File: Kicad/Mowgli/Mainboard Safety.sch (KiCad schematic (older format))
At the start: 3 parts, among them U3 4075

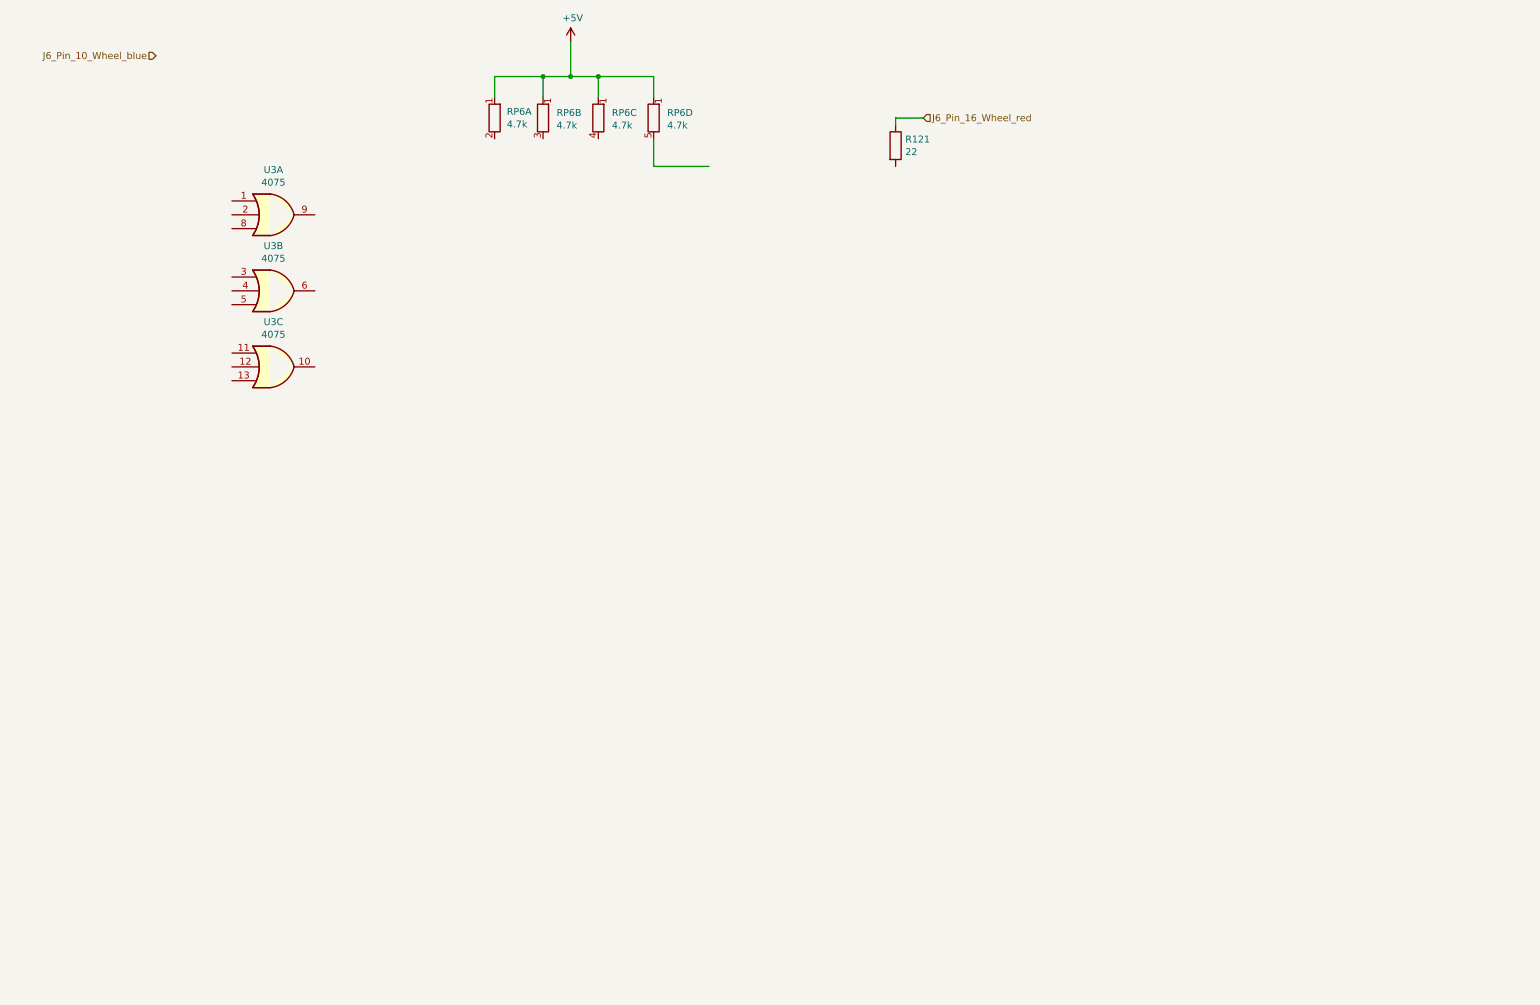
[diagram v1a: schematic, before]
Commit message: reversed mechanical tilt and accelerometer circuit
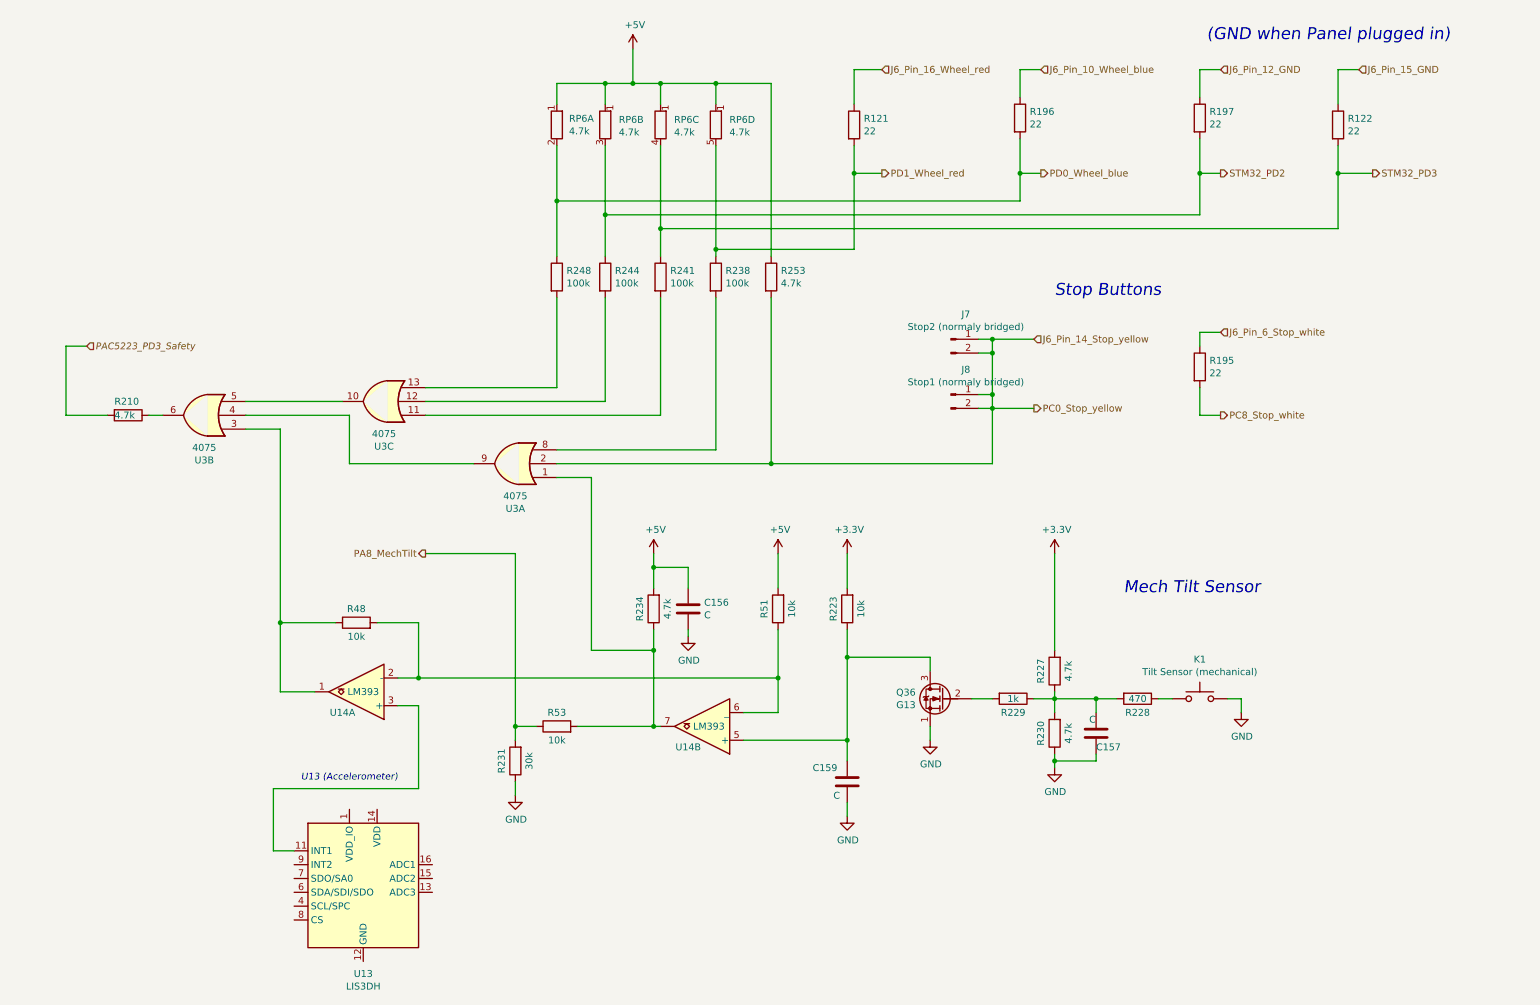
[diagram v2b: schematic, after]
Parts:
- added C156, C157, C159: C, symbol Device:C
- added J7: Stop2 (normaly bridged), symbol Connector:Conn_01x02_Male
- added J8: Stop1 (normaly bridged), symbol Connector:Conn_01x02_Male
- added K1: Tilt Sensor (mechanical), symbol Switch:SW_Push
- added Q36: G13, symbol Device:Q_NMOS_SGD
- added R122, R195, R196, R197: 22, symbol Device:R
- added R210, R227, R230, R234, R253: 4.7k, symbol Device:R
- added R223, R48, R51, R53: 10k, symbol Device:R
- added R228: 470, symbol Device:R
- added R229: 1k, symbol Device:R
- added R231: 30k, symbol Device:R
- added R238, R241, R244, R248: 100k, symbol Device:R
- added U13: LIS3DH, Package_LGA:LGA-16_3x3mm_P0.5mm_LayoutBorder3x5y, symbol Sensor_Motion:LIS3DH
- added U14: LM393, symbol Comparator:LM393
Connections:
- net labels added: +3.3V, GND, J6_Pin_12_GND, J6_Pin_14_Stop_yellow, J6_Pin_15_GND, J6_Pin_6_Stop_white, PA8_MechTilt, PAC5223_PD3_Safety, PC0_Stop_yellow, PC8_Stop_white, PD0_Wheel_blue, PD1_Wheel_red, STM32_PD2, STM32_PD3
- wire segments 13 -> 135
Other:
- note added: "(GND when Panel plugged in)"
- note added: "Mech Tilt Sensor"
- note added: "Stop Buttons"
- note added: "U13 (Accelerometer)"
- moved on the sheet: R121, RP6A, RP6B, RP6C, RP6D, U3A, U3B, U3C

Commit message: added Panel Eliminator
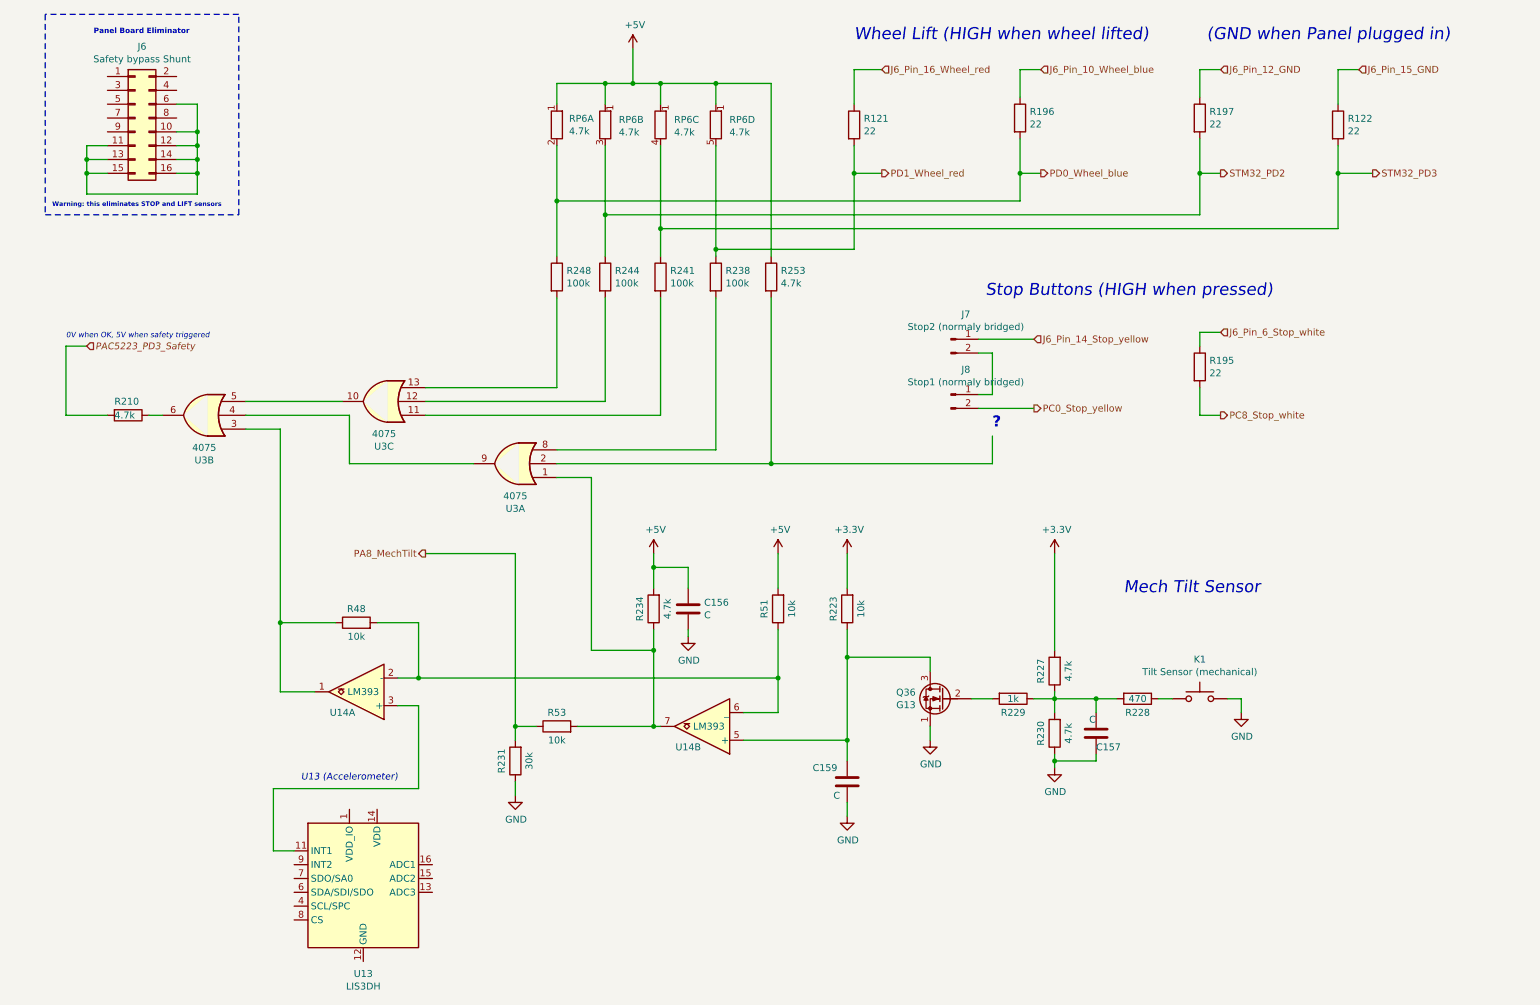
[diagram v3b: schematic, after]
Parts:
- added J6: Safety bypass Shunt, symbol Connector_Generic:Conn_02x08_Odd_Even
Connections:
- wire segments 135 -> 148
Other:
- note added: "0V when OK, 5V when safety triggered"
- note added: "?"
- note added: "Panel Board Eliminator"
- note added: "Stop Buttons (HIGH when pressed)"
- note added: "Warning: this eliminates STOP and LIFT sensors"
- note added: "Wheel Lift (HIGH when wheel lifted)"
- note removed: "Stop Buttons"
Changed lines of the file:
@@
 	7500 3050 7600 3050
 Wire Wire Line
-	7500 2950 7600 2950
-Wire Wire Line
-	7600 3050 7600 2950
-Connection ~ 7600 2950
-Wire Wire Line
-	7600 2950 7900 2950
-Wire Wire Line
 	7600 3050 7600 3350
 Wire Wire Line
 	7600 3350 7500 3350
-Connection ~ 7600 3050
 Text HLabel 7900 3450 2    50   Output ~ 0
 PC0_Stop_yellow
-Wire Wire Line
-	7900 3450 7600 3450
 $Comp
 L Device:R R253
@@
 	1    0    0    -1
 $EndComp
-Connection ~ 7600 3450
 $Comp
 L Device:R R238
@@
 $EndComp
 Wire Wire Line
-	7600 3450 7600 3850
-Wire Wire Line
 	4450 3850 6000 3850
 Wire Wire Line
@@
 Wire Wire Line
 	5200 2150 10100 2150
-Text Notes 8050 2650 0    87   Italic 0
-Stop Buttons
-Wire Wire Line
-	7600 3350 7600 3450
-Connection ~ 7600 3350
-Wire Wire Line
-	7500 3450 7600 3450
+Text Notes 7550 2650 0    87   Italic 0
+Stop Buttons (HIGH when pressed)
 Wire Wire Line
 	3500 4500 4150 4500
@@
 Wire Wire Line
 	900  3500 1200 3500
+Text Notes 900  2950 0    39   Italic 0
+0V when OK, 5V when safety triggered
+Wire Wire Line
+	7500 2950 7900 2950
+Wire Wire Line
+	7500 3450 7900 3450
+Wire Wire Line
+	7600 3650 7600 3850
+Text Notes 7600 3600 0    79   ~ 16
+?
+Text Notes 6600 800  0    87   Italic 0
+Wheel Lift (HIGH when wheel lifted)
+$Comp
+L Connector_Generic:Conn_02x08_Odd_Even J6
+U 1 1 62E3115A
+P 1400 1350
+F 0 "J6" H 1450 1867 50  0000 C CNN
+F 1 "Safety bypass Shunt" H 1450 1776 50  0000 C CNN
+F 2 "" H 1400 1350 50  0001 C CNN
+F 3 "~" H 1400 1350 50  0001 C CNN
+	1    1400 1350
+	1    0    0    -1
+$EndComp
+Wire Wire Line
+	1700 1450 1850 1450
+Wire Wire Line
+	1850 1450 1850 1550
+Wire Wire Line
+	1850 1750 1700 1750
+Wire Wire Line
+	1700 1650 1850 1650
+Connection ~ 1850 1650
+Wire Wire Line
+	1850 1650 1850 1750
+Wire Wire Line
+	1700 1550 1850 1550
+Connection ~ 1850 1550
+Wire Wire Line
+	1850 1550 1850 1650
+Wire Wire Line
+	1700 1250 1850 1250
+Wire Wire Line
+	1850 1250 1850 1450
+Connection ~ 1850 1450
+Wire Wire Line
+	1200 1550 1050 1550
+Wire Wire Line
+	1050 1550 1050 1650
+Wire Wire Line
+	1050 1750 1200 1750
+Wire Wire Line
+	1200 1650 1050 1650
+Connection ~ 1050 1650
+Wire Wire Line
+	1050 1650 1050 1750
+Wire Wire Line
+	1050 1750 1050 1900
+Wire Wire Line
+	1050 1900 1850 1900
+Wire Wire Line
+	1850 1900 1850 1750
+Connection ~ 1050 1750
+Connection ~ 1850 1750
+Text Notes 1100 750  0    39   ~ 8
+Panel Board Eliminator
+Wire Notes Line
+	750  600  750  2050
+Wire Notes Line
+	750  2050 2150 2050
+Wire Notes Line
+	2150 2050 2150 600
+Wire Notes Line
+	2150 600  750  600
+Text Notes 800  2000 0    33   ~ 7
+Warning: this eliminates STOP and LIFT sensors
 $EndSCHEMATC

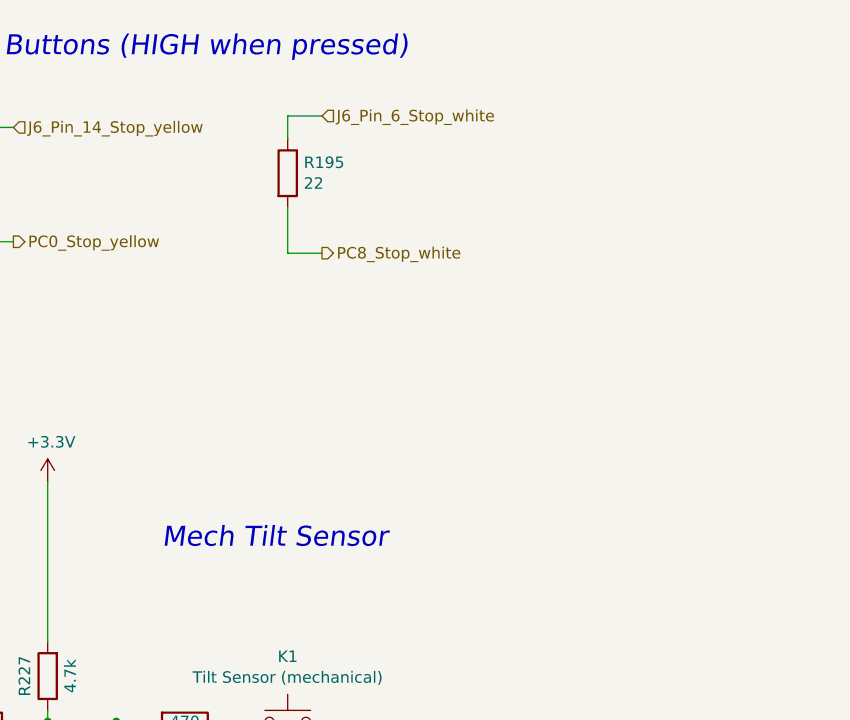
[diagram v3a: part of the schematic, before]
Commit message: R195 is not populated on all boards, (white hall sensor cable for stop button)
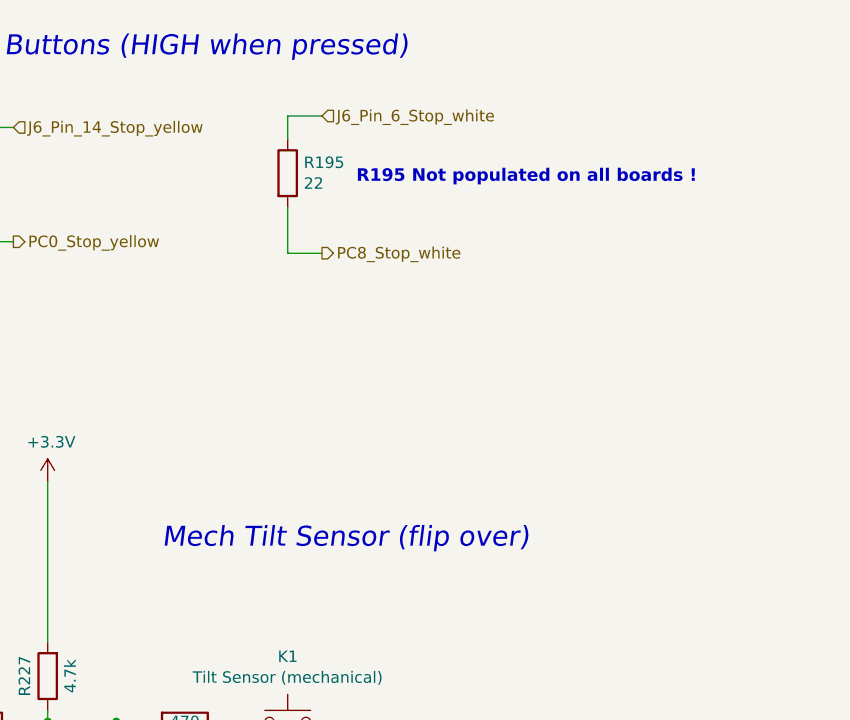
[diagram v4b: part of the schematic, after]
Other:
- note added: "Mech Tilt Sensor (flip over)"
- note added: "R195 Not populated on all boards !"
- note removed: "Mech Tilt Sensor"
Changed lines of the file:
@@
 	8050 4500 8050 5200
 Text Notes 8550 4800 0    87   Italic 0
-Mech Tilt Sensor
+Mech Tilt Sensor (flip over)
 $Comp
 L Sensor_Motion:LIS3DH U13
@@
 Text Notes 800  2000 0    33   ~ 7
 Warning: this eliminates STOP and LIFT sensors
+Text Notes 9400 3200 0    55   ~ 11
+R195 Not populated on all boards !
 $EndSCHEMATC
